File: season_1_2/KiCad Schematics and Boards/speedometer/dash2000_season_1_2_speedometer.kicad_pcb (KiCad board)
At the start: 2 copper layers, 152.4 x 116.8 mm, 46 parts, among them U1 LM2576HVS-3.3, U10 SA39-11SRWA, U11 SA39-11SRWA, U12 SA39-11SRWA, U13 SA39-11SRWA, U14 SA39-11SRWA, U15 SA39-11SRWA, U16 SA39-11SRWA, U17 SA39-11SRWA, U18 SA39-11SRWA, U19 SA39-11SRWA, U2 ESP32-S3-WROOM-1, U3 MCP2517FD-xSL, U4 SN65HVD230, U5 LED1642GWTTR, U6 SA39-11SRWA, U7 SA39-11SRWA, U8 SA39-11SRWA, U9 SA39-11SRWA

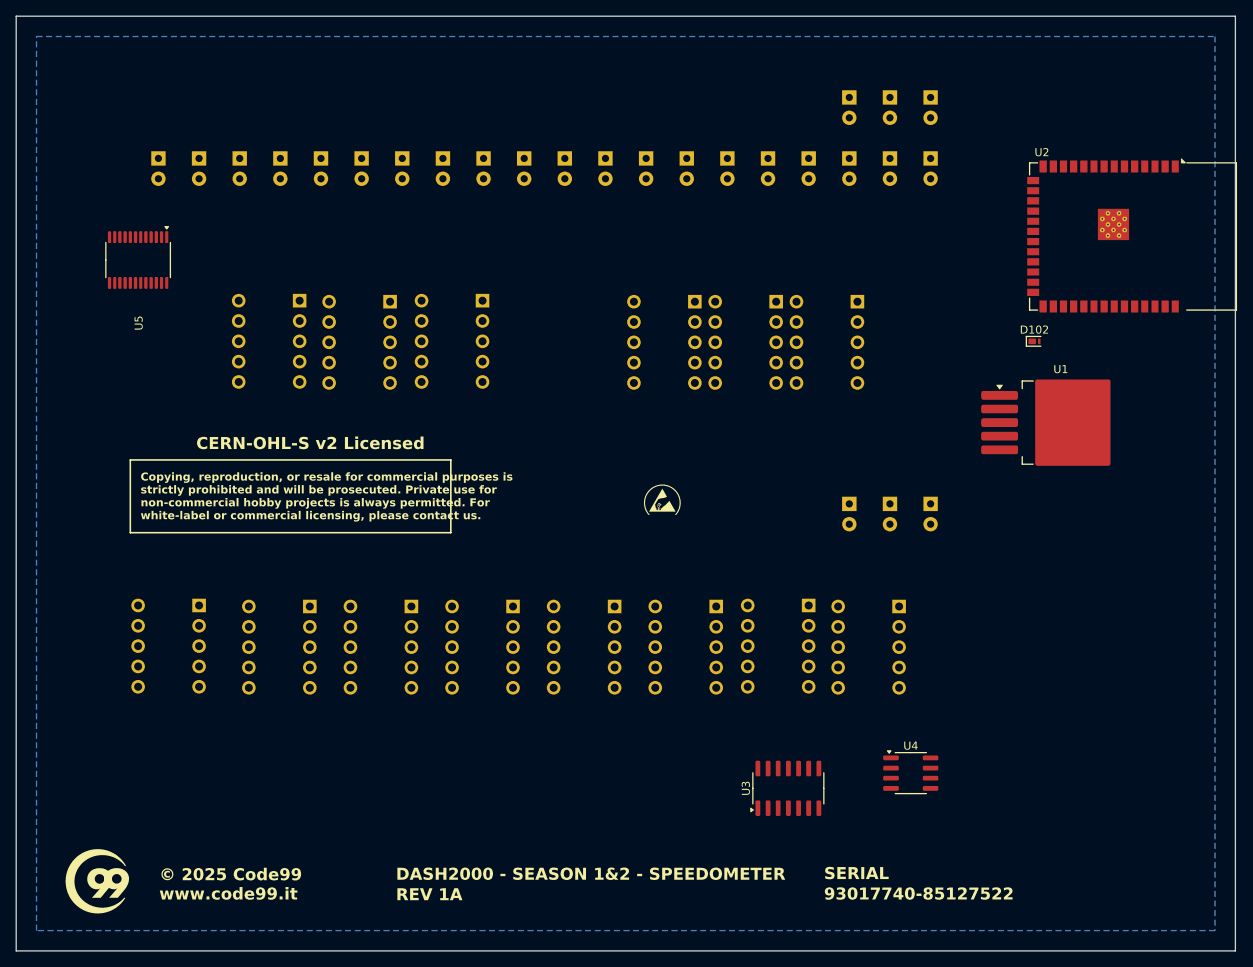
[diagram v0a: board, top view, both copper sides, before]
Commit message: Added lots of electronic devices and routes
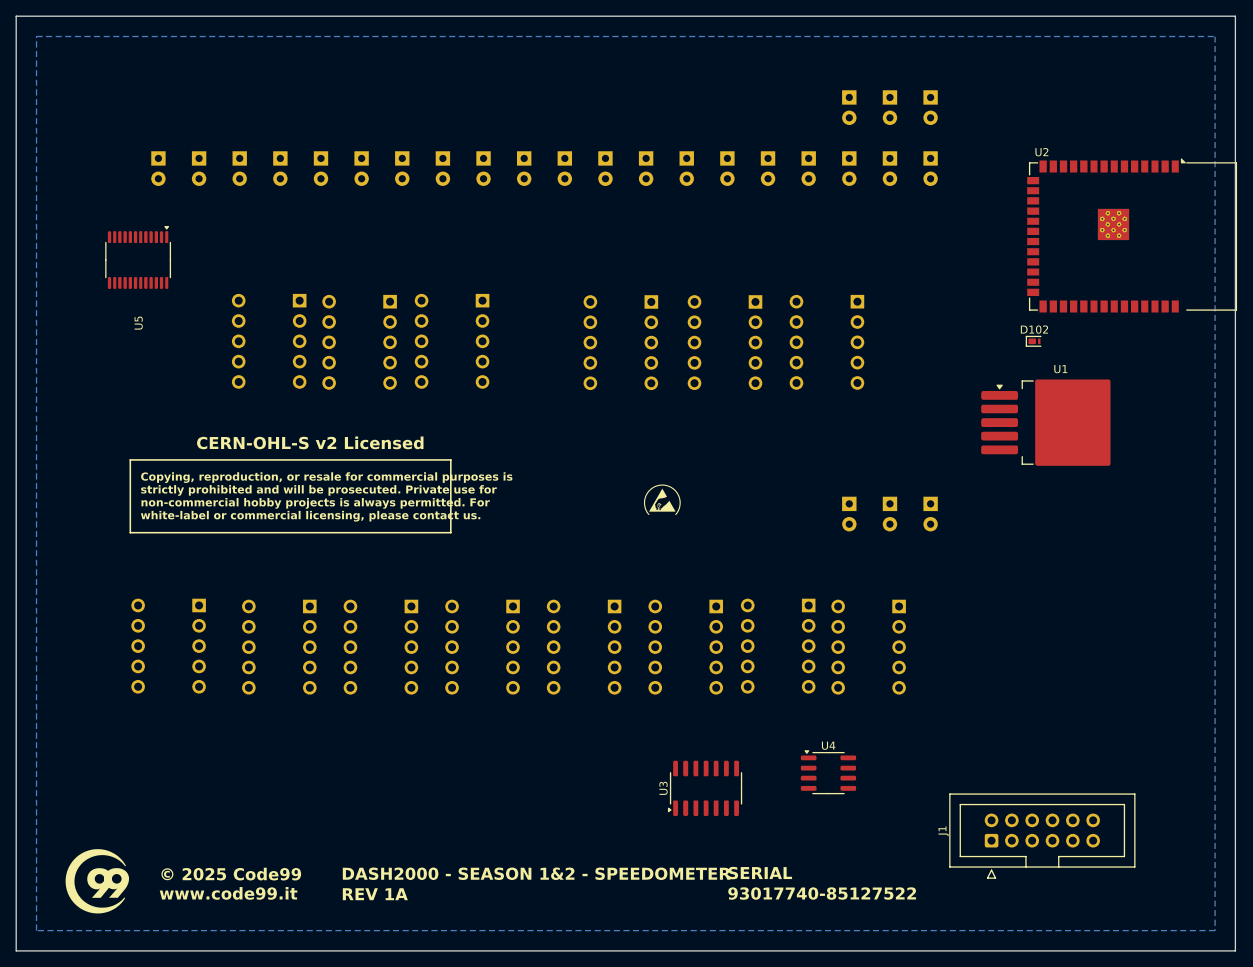
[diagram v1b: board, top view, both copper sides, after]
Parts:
- added J1: Conn_02x06_Top_Bottom, Connector_IDC:IDC-Header_2x06_P2.54mm_Vertical, F.Cu at (142.2, 136.1)
- moved U3 10.3 mm to (106.5, 129.5)
- moved U4 10.3 mm to (121.9, 127.6)
- moved U11 5.44 mm to (99.7, 68.7)
- moved U10 2.58 mm to (112.7, 68.7)
